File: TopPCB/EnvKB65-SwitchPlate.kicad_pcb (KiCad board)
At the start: 2 copper layers, 326.8 x 101 mm, 11 parts

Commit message: updated gerbers
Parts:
- added G***: LOGO, Logo:patern, F.Cu at (225.5, 148.3)

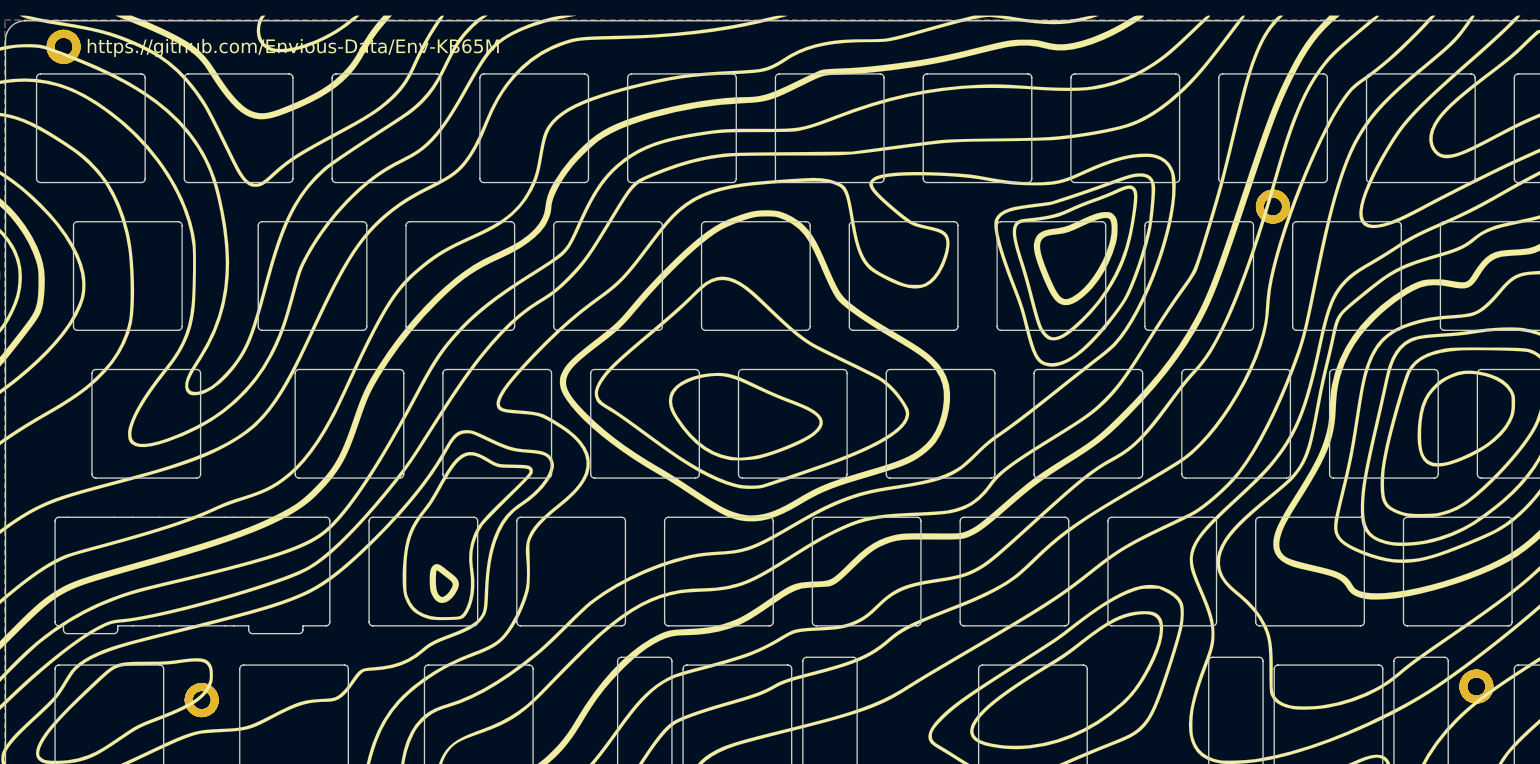
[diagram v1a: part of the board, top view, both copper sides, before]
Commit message: fixed duplicated mount holes
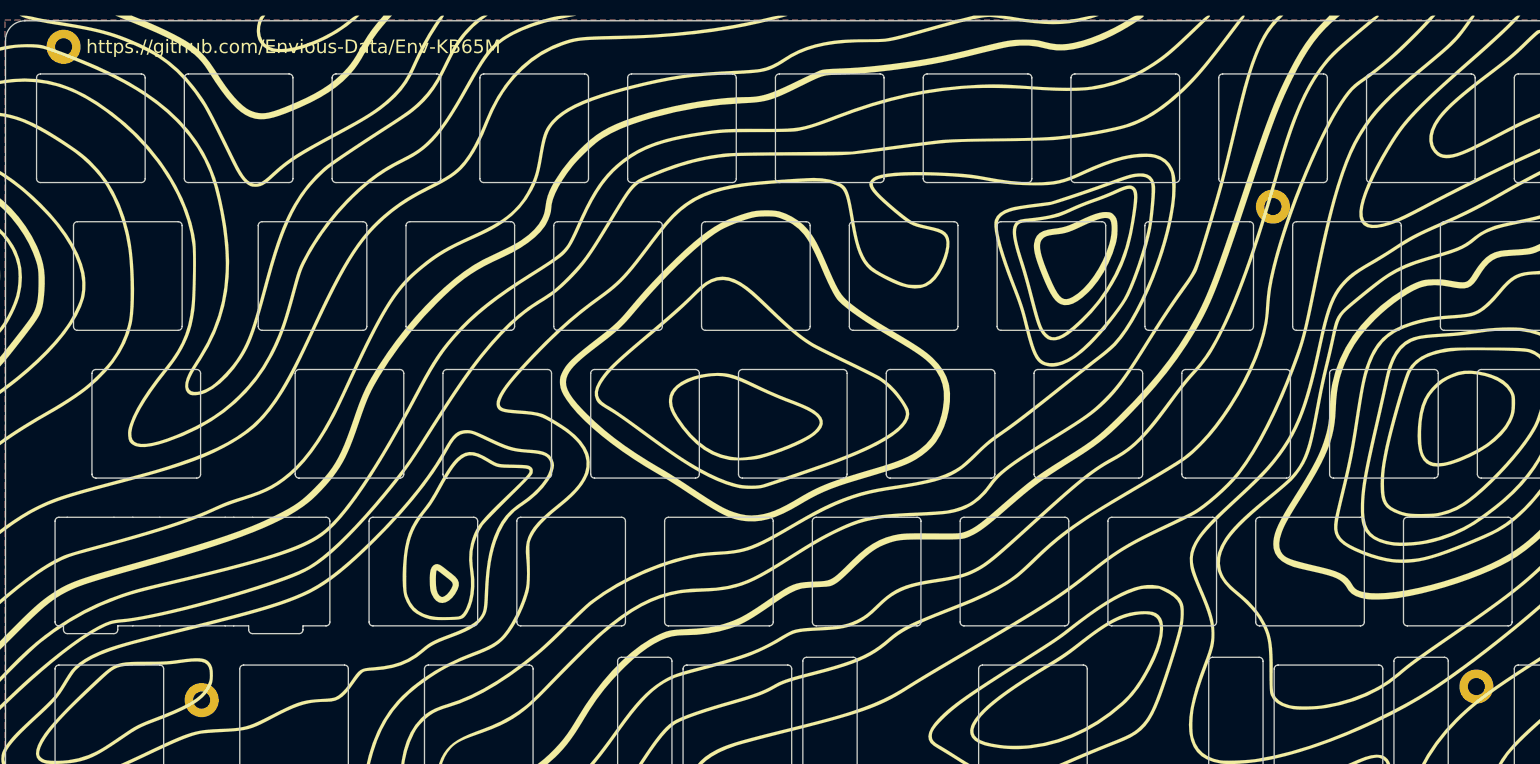
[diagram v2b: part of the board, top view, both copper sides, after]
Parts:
- removed the H2 at (69.0, 101.0)
- removed the H3 at (86.8, 185.2)
- removed the H5 at (224.9, 121.6)
- removed the H6 at (251.1, 183.5)
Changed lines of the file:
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@@
-      (net 1 "GND"))
-  )
-  (footprint "MountingHole:MountingHole_2.2mm_M2_Pad" (layer "F.Cu")
-    (at 69.0005 101)
-    (descr "Mounting Hole 2.2mm, M2")
-    (tags "mounting hole 2.2mm m2")
-    (attr exclude_from_pos_files exclude_from_bom)
-    (fp_text reference "H2" (at 0 -3.2) (layer "F.Fab")
-      (effects (font (size 1 1) (thickness 0.15)))
-    )
-    (fp_text value "MountingHole" (at 0 3.2) (layer "F.Fab")
-      (effects (font (size 1 1) (thickness 0.15)))
-    )
-    (fp_text user "${REFERENCE}" (at 0.3 0) (layer "F.Fab")
-      (effects (font (size 1 1) (thickness 0.15)))
-    )
-    (fp_circle (center 0 0) (end 2.2 0) (layer "Cmts.User") (width 0.15) (fill none))
-    (fp_circle (center 0 0) (end 2.45 0) (layer "F.CrtYd") (width 0.05) (fill none))
-    (pad "1" thru_hole circle locked (at 0 0) (size 4.4 4.4) (drill 2.2) (layers *.Cu *.Mask)
-      (net 1 "GND"))
-  )
-  (footprint "MountingHole:MountingHole_2.2mm_M2_Pad" (layer "F.Cu")
-    (at 86.8005 185.22)
-    (descr "Mounting Hole 2.2mm, M2")
-    (tags "mounting hole 2.2mm m2")
-    (attr exclude_from_pos_files exclude_from_bom)
-    (fp_text reference "H3" (at 0 -3.2) (layer "F.Fab")
-      (effects (font (size 1 1) (thickness 0.15)))
-    )
-    (fp_text value "MountingHole" (at 0 3.2) (layer "F.Fab")
-      (effects (font (size 1 1) (thickness 0.15)))
-    )
-    (fp_text user "${REFERENCE}" (at 0.3 0) (layer "F.Fab")
-      (effects (font (size 1 1) (thickness 0.15)))
-    )
-    (fp_circle (center 0 0) (end 2.2 0) (layer "Cmts.User") (width 0.15) (fill none))
-    (fp_circle (center 0 0) (end 2.45 0) (layer "F.CrtYd") (width 0.05) (fill none))
-    (pad "1" thru_hole circle locked (at 0 0) (size 4.4 4.4) (drill 2.2) (layers *.Cu *.Mask)
-      (net 1 "GND"))
-  )
-  (footprint "MountingHole:MountingHole_2.2mm_M2_Pad" (layer "F.Cu")
-    (at 224.9005 121.6)
-    (descr "Mounting Hole 2.2mm, M2")
-    (tags "mounting hole 2.2mm m2")
-    (attr exclude_from_pos_files exclude_from_bom)
-    (fp_text reference "H5" (at 0 -3.2) (layer "F.Fab")
-      (effects (font (size 1 1) (thickness 0.15)))
-    )
-    (fp_text value "MountingHole" (at 0 3.2) (layer "F.Fab")
-      (effects (font (size 1 1) (thickness 0.15)))
-    )
-    (fp_text user "${REFERENCE}" (at 0.3 0) (layer "F.Fab")
-      (effects (font (size 1 1) (thickness 0.15)))
-    )
-    (fp_circle (center 0 0) (end 2.2 0) (layer "Cmts.User") (width 0.15) (fill none))
-    (fp_circle (center 0 0) (end 2.45 0) (layer "F.CrtYd") (width 0.05) (fill none))
-    (pad "1" thru_hole circle locked (at 0 0) (size 4.4 4.4) (drill 2.2) (layers *.Cu *.Mask)
-      (net 1 "GND"))
-  )
-  (footprint "MountingHole:MountingHole_2.2mm_M2_Pad" (layer "F.Cu")
-    (at 251.12525 183.475)
-    (descr "Mounting Hole 2.2mm, M2")
-    (tags "mounting hole 2.2mm m2")
-    (attr exclude_from_pos_files exclude_from_bom)
-    (fp_text reference "H6" (at 0 -3.2) (layer "F.Fab")
-      (effects (font (size 1 1) (thickness 0.15)))
-    )
-    (fp_text value "MountingHole" (at 0 3.2) (layer "F.Fab")
-      (effects (font (size 1 1) (thickness 0.15)))
-    )
-    (fp_text user "${REFERENCE}" (at 0.3 0) (layer "F.Fab")
-      (effects (font (size 1 1) (thickness 0.15)))
-    )
-    (fp_circle (center 0 0) (end 2.2 0) (layer "Cmts.User") (width 0.15) (fill none))
-    (fp_circle (center 0 0) (end 2.45 0) (layer "F.CrtYd") (width 0.05) (fill none))
-    (pad "1" thru_hole circle locked (at 0 0) (size 4.4 4.4) (drill 2.2) (layers *.Cu *.Mask)
       (net 1 "GND"))
   )
